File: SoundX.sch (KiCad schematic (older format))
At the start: 30 parts, among them CN1 EDGE_CONN, CN2 RAW_AUDIO_OUT, U2 GAL20V8, U3 YM3526, U6 YM3014, U7 LM324, Y1 OSCILLATOR

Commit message: Rough routing complete, even not that rough
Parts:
- added C11: 100n, Capacitor_THT:C_Disc_D7.0mm_W2.5mm_P5.00mm, symbol Device:C
- added CN3: CONN_MIDI_IN, SoundX:DIN5, symbol Connector:DIN-5_180degree
- added CN4: CONN_MIDI_OUT, SoundX:DIN5, symbol Connector:DIN-5_180degree
- added D1: 1n4148, Diode_THT:D_DO-35_SOD27_P2.54mm_Vertical_KathodeUp, symbol Device:D
- added JP3: JMP_POM_GND, Jumper:SolderJumper-2_P1.3mm_Open_RoundedPad1.0x1.5mm, symbol Device:Jumper_NO_Small
- added JP4: JMP_POM_VCC, Jumper:SolderJumper-2_P1.3mm_Open_RoundedPad1.0x1.5mm, symbol Device:Jumper_NO_Small
- added R10, R11, R12, R8: 220, Resistor_THT:R_Axial_DIN0207_L6.3mm_D2.5mm_P2.54mm_Vertical, symbol Device:R
- added R9: 4.7k, Resistor_THT:R_Axial_DIN0207_L6.3mm_D2.5mm_P2.54mm_Vertical, symbol Device:R
- added U2: MOS_6551_ACIA, Package_DIP:DIP-28_W15.24mm_Socket_LongPads, symbol W65C51S:W65C51S
- added U4: 6N138, Package_DIP:DIP-8_W7.62mm_Socket_LongPads, symbol Isolator:6N138
- added Y2: 3M, Crystal:Crystal_HC49-U_Vertical, symbol Device:Crystal
- R15, R16, R3, R4, R5, R6, R7: footprint Resistor_THT:R_Axial_DIN0207_L6.3mm_D2.5mm_P10.16mm_Horizontal -> Resistor_THT:R_Axial_DIN0207_L6.3mm_D2.5mm_P2.54mm_Vertical
- Y1: value OSCILLATOR -> 3.579545 MHz
- renumbered U2 to U1
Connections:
- net +5V: now also C11.1, JP4.1, R10.2, R12.2, U2.15 (VCC), U2.2 (CS0), U4.8 (VCC)
- net GND: now also C11.2, CN4.2, JP3.1, R9.1, U2.1 (GND), U2.16 (~DCD), U2.17 (~DSR), U2.9 (~CTS), U4.5 (GND)
- net a0: now also U2.13 (RS0)
- net a1: now also U2.14 (RS1)
- net a9: now also U1.19 (IO19); no longer U1.21 (IO21)
- net d0: now also U2.18 (D0)
- net d1: now also U2.19 (D1)
- net d2: now also U2.20 (D2)
- net d3: now also U2.21 (D3)
- net d4: now also U2.22 (D4)
- net d5: now also U2.23 (D5)
- net d6: now also U2.24 (D6)
- net d7: now also U2.25 (D7)
- net phi2: now also U2.27 (PHI2)
- net r_~w: now also U2.28 (R_~W)
- net ~irq: now also U2.26 (~IRQ)
- net ~reset: now also U2.4 (~RESET)
- net ~ym_cs: now also U1.20 (I020); no longer U1.19 (IO19)
- net ~ym_rd: now also U1.21 (IO21); no longer U1.20 (I020)
- net at R15.2, U6.8 (MP), U7.13 (-)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: now also R5.1; no longer R5.2
- net at C1.1, R16.2, U7.7: now also R6.1; no longer R6.2
- net ~kbd_cs renamed ~midi_cs
- net ~midi_cs: now also U2.3 (~CS1)
- new net: U2.7 (XTLO), Y2.1
- new net: U2.6 (XTLI), Y2.2
- new net: CN4.1, JP4.2
- new net: CN4.3, JP3.2
- new net: CN4.4, R12.1
- new net: CN4.5, R11.2
- new net: CN3.4, R8.1
- new net: D1.1 (K), R8.2, U4.2 (C1)
- new net: CN3.5, D1.2 (A), U4.3 (C2)
- new net: R9.2, U4.7 (VO1)
- new net: R5.2, R6.2, U7.6 (-)
- new net rxd_ttl: R10.1, U2.12 (RXD), U4.6 (VO2)
- new net txd_ttl: R11.1, U2.10 (TXD)
- no-connect marks 14 -> 19
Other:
- note added: "(NTSC color subcarrier frequency)\n\n520-TCF357-X (DIP-14)\nOR\n520-TCH357-X (DIP-8)"
- note added: "1K may\nbe better"
- note added: "MIDI INPUT"
- note added: "MIDI OUTPUT"
- note added: "NOTE 3 MHZ CRYSTAL!\nTHIS ALLOWS REACHING THE\n31250 BPS REQUIRED FOR MIDI\nCONFIGURING THE ACIA FOR 19200 BPS\n(DIVISOR = 96 => 3000000/96 = 31250)"
- note added: "POWER-OVER-MIDI JUMPERS\nTAKEN FROM SPARKFUN\nMIDI SHIELD"
- note added: "RS-232 INTERFACE\n(TTL LEVEL)"
- note removed: "3.579545 MHz\n(NTSC color subcarrier frequency)\n\n520-TCF357-X (DIP-14)\nOR\n520-TCH357-X (DIP-8)"

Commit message: First round of improvements by @kinmami
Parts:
- added C12: 22p, Capacitor_THT:C_Disc_D7.0mm_W2.5mm_P5.00mm, symbol Device:C
- added C13: 220p, Capacitor_THT:C_Disc_D7.0mm_W2.5mm_P5.00mm, symbol Device:C
- added C14: 100n, Capacitor_THT:C_Disc_D7.0mm_W2.5mm_P5.00mm, symbol Device:C
- added C15: 10u, Capacitor_THT:CP_Radial_D5.0mm_P2.00mm, symbol Device:CP1
- added FB1: FERRITE, Inductor_THT:L_Radial_D6.0mm_P4.00mm, symbol Device:Ferrite_Bead_Small
- added R1: 1M, Resistor_THT:R_Axial_DIN0207_L6.3mm_D2.5mm_P2.54mm_Vertical, symbol Device:R
- C1: value 4.7u -> 10u
- R16: value 4.7k -> 10k
- renumbered FB1 to FB2, FB2 to FB3
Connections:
- net +5V: now also C15.1, FB1.2; no longer CN1.2 (VCC), CN1.3 (VCC)
- net GND: now also C12.2, C13.2, C14.2, C15.2
- net clock: now also FB3.1; no longer R7.1
- net q-: now reaches U2.7 (XTLO), Y2.1
- net q-: now also R1.1
- net q+: now reaches U2.6 (XTLI), Y2.2
- net q+: now also C12.1, R1.2
- net at Y1.8 (OUT): now also R7.2; no longer FB3.2
- net at C6.1, R3.2, R4.1: now also C13.1
- new net: C14.1, CN1.2 (VCC), CN1.3 (VCC), FB1.1
- new net: FB3.2, R7.1
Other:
- note added: "NOTE 3 MHZ CRYSTAL!\nTHIS ALLOWS REACHING THE\n31250 BPS REQUIRED FOR MIDI\nCONFIGURING THE ACIA FOR 19200 BPS\n(DIVISOR = 96 => 3000000/96 = 31250)\n\nWE ALSO PROVIDE PARALLEL R AND\nSERIES C FOR W65C51S, BUT I'D\nRECOMMEND USING AN OLDER 6551"
- note removed: "NOTE 3 MHZ CRYSTAL!\nTHIS ALLOWS REACHING THE\n31250 BPS REQUIRED FOR MIDI\nCONFIGURING THE ACIA FOR 19200 BPS\n(DIVISOR = 96 => 3000000/96 = 31250)"
- moved on the sheet: C4, C7, C8, C9, FB3, R7, U7E, Y2

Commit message: Add logo
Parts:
- V1: footprint (none) -> SoundX:logo
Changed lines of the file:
@@
 F 0 "V1" H 15288 9751 50  0000 L CNN
 F 1 "LOGO" H 15288 9660 50  0000 L CNN
-F 2 "" H 15210 9705 50  0001 C CNN
+F 2 "SoundX:logo" H 15210 9705 50  0001 C CNN
 F 3 "" H 15210 9705 50  0001 C CNN
 F 4 "-" H 15210 9705 50  0001 C CNN "MouserPN"

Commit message: Add filter bypass jumper
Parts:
- added JP5: JMP_FILTER_BYPASS, Jumper:SolderJumper-3_P1.3mm_Open_RoundedPad1.0x1.5mm, symbol Jumper:Jumper_3_Open
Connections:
- net at R3.1, U7.1, U7.2 (-): now also JP5.3 (B)
- net at C6.2, U7.8, U7.9 (-): now also JP5.1 (A); no longer U7.5 (+)
- new net amp_in: JP5.2 (C), U7.5 (+)
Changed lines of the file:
@@
 Wire Wire Line
 	11280 6370 11200 6370
-Wire Wire Line
-	11280 6370 11525 6370
-Wire Wire Line
-	11525 6370 11525 6455
-Wire Wire Line
-	11525 6455 11665 6455
 Connection ~ 11280 6370
 Wire Wire Line
@@
 Text Notes 10430 6995 0    50   ~ 0
 15 KHz LOW-PASS FILTER
-Text Notes 11785 6855 0    50   ~ 0
+Text Notes 11770 6995 0    50   ~ 0
 AMPLIFIER
 Text Label 7845 5195 2    50   ~ 0
@@
 	1    0    0    -1
 $EndComp
+$Comp
+L Device:CP1 C?
+U 1 1 65AC9FB0
+P 5560 10250
+AR Path="/6579482E/65AC9FB0" Ref="C?"  Part="1"
+AR Path="/65AC9FB0" Ref="C15"  Part="1"
+F 0 "C15" H 5675 10296 50  0000 L CNN
+F 1 "10u" H 5675 10205 50  0000 L CNN
+F 2 "Capacitor_THT:CP_Radial_D5.0mm_P2.00mm" H 5560 10250 50  0001 C CNN
+F 3 "~" H 5560 10250 50  0001 C CNN
+	1    5560 10250
+	1    0    0    -1
+$EndComp
+$Comp
+L Jumper:Jumper_3_Open JP5
+U 1 1 65B030FE
+P 11420 6455
+F 0 "JP5" V 11130 6300 50  0000 L CNN
+F 1 "JMP_FILTER_BYPASS" V 11050 6030 50  0000 L CNN
+F 2 "Jumper:SolderJumper-3_P1.3mm_Open_RoundedPad1.0x1.5mm" H 11420 6455 50  0001 C CNN
+F 3 "~" H 11420 6455 50  0001 C CNN
+	1    11420 6455
+	0    -1   -1   0
+$EndComp
+Wire Wire Line
+	11570 6455 11665 6455
+Wire Wire Line
+	11280 6370 11340 6370
+Wire Wire Line
+	11340 6370 11340 6765
+Wire Wire Line
+	11340 6765 11420 6765
+Wire Wire Line
+	11420 6765 11420 6705
+Wire Wire Line
+	11420 6205 11420 5950
+Wire Wire Line
+	9415 5950 9415 6270
+Wire Wire Line
+	9415 5950 11420 5950
 Wire Bus Line
 	5505 5895 5505 6595
@@
 Wire Bus Line
 	12565 1780 12565 3725
-$Comp
-L Device:CP1 C?
-U 1 1 65AC9FB0
-P 5560 10250
-AR Path="/6579482E/65AC9FB0" Ref="C?"  Part="1"
-AR Path="/65AC9FB0" Ref="C15"  Part="1"
-F 0 "C15" H 5675 10296 50  0000 L CNN
-F 1 "10u" H 5675 10205 50  0000 L CNN
-F 2 "Capacitor_THT:CP_Radial_D5.0mm_P2.00mm" H 5560 10250 50  0001 C CNN
-F 3 "~" H 5560 10250 50  0001 C CNN
-	1    5560 10250
-	1    0    0    -1
-$EndComp
+Text Label 11665 6455 2    50   ~ 0
+amp_in
 $EndSCHEMATC

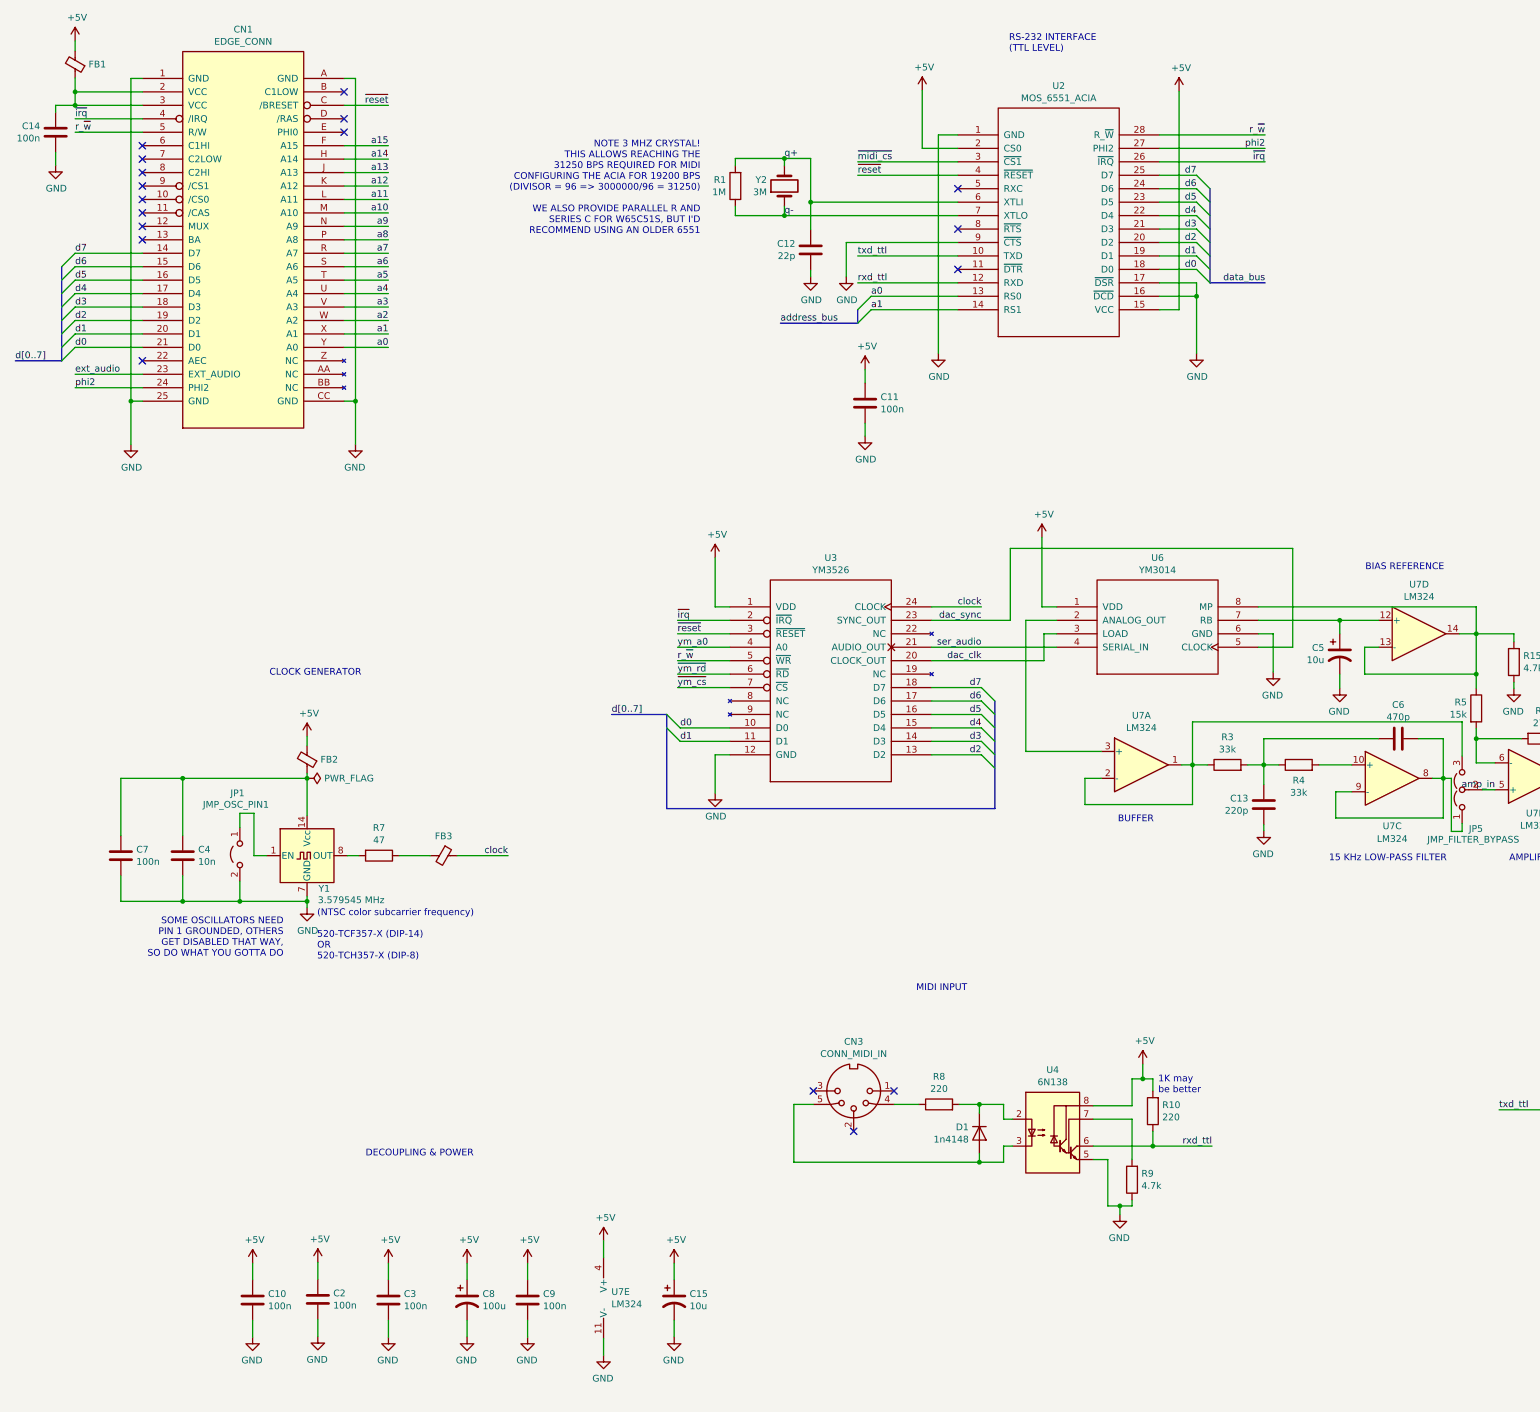
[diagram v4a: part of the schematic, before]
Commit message: Tidy up silkscreen
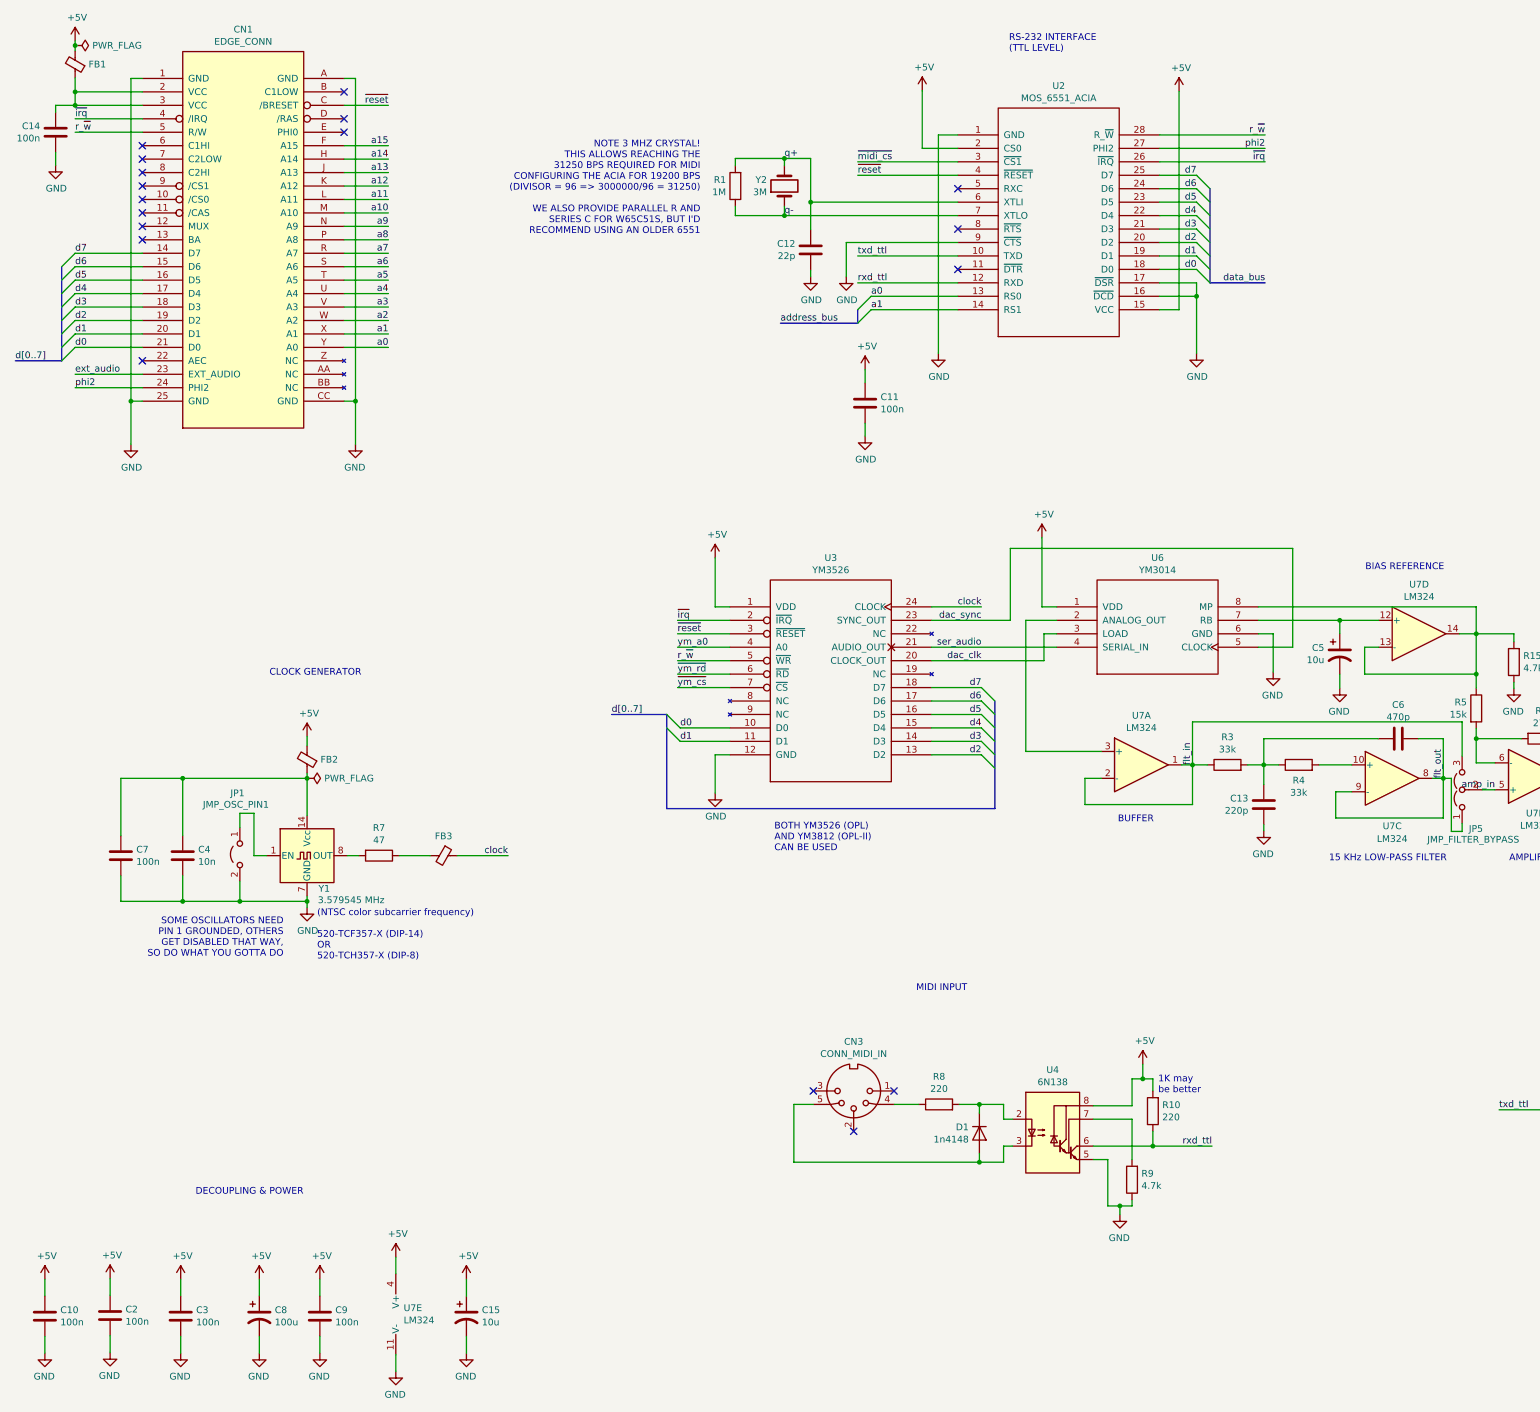
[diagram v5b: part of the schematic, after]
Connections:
- net flt_out: now reaches C6.2, JP5.1 (A), U7.8, U7.9 (-)
- net flt_in: now reaches JP5.3 (B), R3.1, U7.1, U7.2 (-)
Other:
- note added: "BOTH YM3526 (OPL)\nAND YM3812 (OPL-II)\nCAN BE USED"
- moved on the sheet: C10, C15, C2, C3, C8, C9, U7E

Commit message: Second round of improvements by @kinmami
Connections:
- net at Y1.8 (OUT): now also R7.1; no longer R7.2
- net at FB3.2: now also R7.2; no longer R7.1
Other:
- moved on the sheet: C1, CN2, JP2, JP5, R16, R5, R6, U7B

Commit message: Add output gain pot
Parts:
- removed R6: 27k, Resistor_THT:R_Axial_DIN0207_L6.3mm_D2.5mm_P2.54mm_Vertical, symbol Device:R
- added RV1: 47k, SoundX:Pot_Bourns_3306P, symbol Device:R_POT
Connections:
- net at R5.2, U7.6 (-): now also RV1.2
- net at C1.1, R16.2, U7.7: now also RV1.1
- no-connect marks 19 -> 20
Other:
- note added: "VARIABLE GAIN FOR\nTHE LAST AMP STAGE"
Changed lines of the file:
@@
 	12145 5295 12285 5295
 Wire Wire Line
-	12480 5115 12145 5115
-Wire Wire Line
 	12145 5115 12145 5295
-Wire Wire Line
-	12780 5115 12990 5115
-Wire Wire Line
-	12990 5115 12990 5395
 Wire Wire Line
 	12990 5395 12885 5395
@@
 Text Label 14665 2085 2    50   ~ 0
 ~ym_cs
-$Comp
-L Device:R R?
-U 1 1 6921A920
-P 12630 5115
-AR Path="/6579482E/6921A920" Ref="R?"  Part="1"
-AR Path="/6921A920" Ref="R6"  Part="1"
-F 0 "R6" V 12423 5115 50  0000 C CNN
-F 1 "27k" V 12514 5115 50  0000 C CNN
-F 2 "Resistor_THT:R_Axial_DIN0207_L6.3mm_D2.5mm_P2.54mm_Vertical" V 12560 5115 50  0001 C CNN
-F 3 "~" H 12630 5115 50  0001 C CNN
-	1    12630 5115
-	0    1    1    0
-$EndComp
 Text Notes 5755 2330 2    50   ~ 0
 NOTE 3 MHZ CRYSTAL!\nTHIS ALLOWS REACHING THE\n31250 BPS REQUIRED FOR MIDI\nCONFIGURING THE ACIA FOR 19200 BPS\n(DIVISOR = 96 => 3000000/96 = 31250)\n\nWE ALSO PROVIDE PARALLEL R AND\nSERIES C FOR W65C51S, BUT I'D\nRECOMMEND USING AN OLDER 6551
@@
 Wire Wire Line
 	11525 5340 11525 5355
+$Comp
+L Device:R_POT RV1
+U 1 1 650E791F
+P 12990 5115
+F 0 "RV1" H 12920 5069 50  0000 R CNN
+F 1 "47k" H 12920 5160 50  0000 R CNN
+F 2 "SoundX:Pot_Bourns_3306P" H 12990 5115 50  0001 C CNN
+F 3 "~" H 12990 5115 50  0001 C CNN
+F 4 "652-3306P-1-473" H 12990 5115 50  0001 C CNN "MouserPN"
+	1    12990 5115
+	-1   0    0    1
+$EndComp
+Wire Wire Line
+	12990 5265 12990 5395
+Wire Wire Line
+	12145 5115 12840 5115
+NoConn ~ 12990 4965
+Text Notes 12620 4825 0    50   ~ 0
+VARIABLE GAIN FOR\nTHE LAST AMP STAGE
 Wire Bus Line
 	5505 5895 5505 6595

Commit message: Add detail of components belonging to OPL or MIDI circuit
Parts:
- C1, C10, C13, C14, C15, C3, C4, C5, C6, C7, C9, CN2, FB2, FB3, JP1, JP2, JP5, R15, R16, R3, R4, R5, R7, RV1, U3, U6, U7, Y1: Notes (none) -> OPL
- C11, C12, CN3, CN4, D1, JP3, JP4, R1, R10, R11, R12, R8, R9, U2, U4, Y2: Notes (none) -> MIDI
- C2, C8, FB1, U1: Notes (none) -> COMMON
- CN1: MouserPN (none) -> -; Notes (none) -> COMMON
- V0, V1: Notes (none) -> -
